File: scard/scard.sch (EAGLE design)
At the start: 7 parts, among them Q1 IRFD9210, X1 COAX

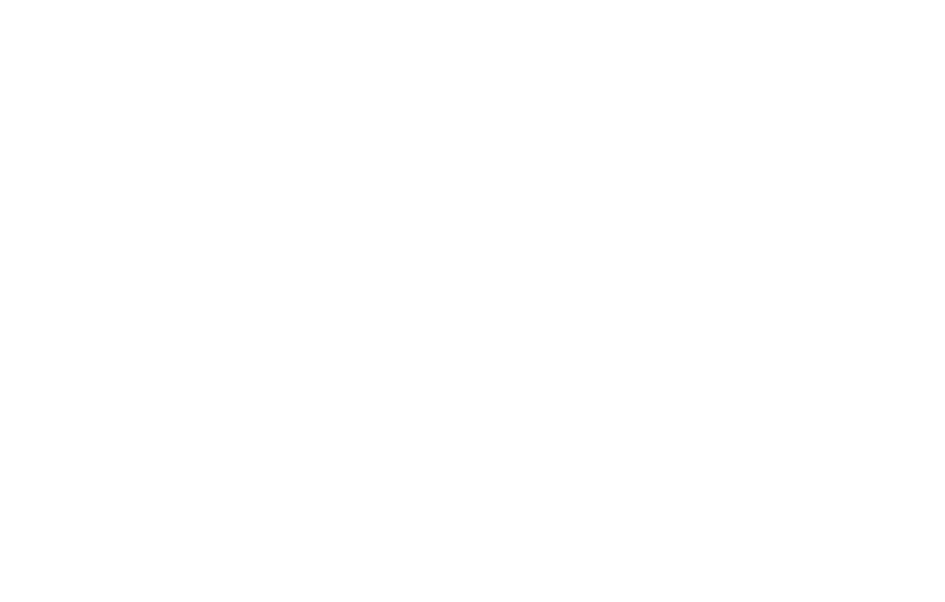
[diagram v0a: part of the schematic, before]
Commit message: added battery charging IC to library
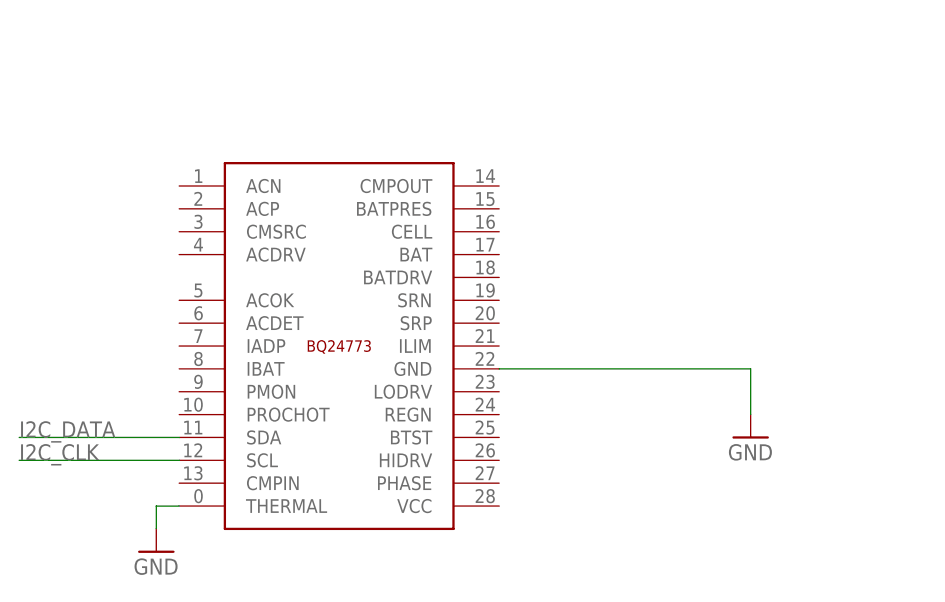
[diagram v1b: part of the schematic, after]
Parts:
- added BQ24773: BQ24773, calsat:BQ24773
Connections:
- new net I2C_CLK: BQ24773.SCL
- new net I2C_DATA: BQ24773.SDA
- net GND: now also BQ24773.GND@1, BQ24773.THERMAL
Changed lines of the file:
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@@
 <part name="GND4" library="supply1" library_urn="urn:adsk.eagle:library:371" deviceset="GND" device=""/>
 <part name="X1" library="con-samtec" library_urn="urn:adsk.eagle:library:184" deviceset="COAX" device=""/>
+<part name="BQ24773" library="calsat" deviceset="BQ24773" device=""/>
+<part name="GND5" library="supply1" library_urn="urn:adsk.eagle:library:371" deviceset="GND" device=""/>
+<part name="GND6" library="supply1" library_urn="urn:adsk.eagle:library:371" deviceset="GND" device=""/>
 </parts>
 <sheets>
@@
 <instance part="GND4" gate="1" x="-167.64" y="81.28"/>
 <instance part="X1" gate="COAX" x="-127" y="129.54"/>
+<instance part="BQ24773" gate="G$1" x="-134.62" y="-66.04"/>
+<instance part="GND5" gate="1" x="-88.9" y="-76.2"/>
+<instance part="GND6" gate="1" x="-154.94" y="-88.9"/>
 </instances>
 <busses>
@@
 <wire x1="-167.64" y1="83.82" x2="-167.64" y2="86.36" width="0.1524" layer="91"/>
 </segment>
+<segment>
+<pinref part="BQ24773" gate="G$1" pin="GND@1"/>
+<wire x1="-116.84" y1="-68.58" x2="-88.9" y2="-68.58" width="0.1524" layer="91"/>
+<wire x1="-88.9" y1="-68.58" x2="-88.9" y2="-73.66" width="0.1524" layer="91"/>
+<pinref part="GND5" gate="1" pin="GND"/>
+</segment>
+<segment>
+<pinref part="BQ24773" gate="G$1" pin="THERMAL"/>
+<pinref part="GND6" gate="1" pin="GND"/>
+<wire x1="-152.4" y1="-83.82" x2="-154.94" y2="-83.82" width="0.1524" layer="91"/>
+<wire x1="-154.94" y1="-83.82" x2="-154.94" y2="-86.36" width="0.1524" layer="91"/>
+</segment>
 </net>
 <net name="STS" class="0">
@@
 </segment>
 </net>
+<net name="I2C_DATA" class="0">
+<segment>
+<pinref part="BQ24773" gate="G$1" pin="SDA"/>
+<wire x1="-152.4" y1="-76.2" x2="-170.18" y2="-76.2" width="0.1524" layer="91"/>
+<label x="-170.18" y="-76.2" size="1.778" layer="95"/>
+</segment>
+</net>
+<net name="I2C_CLK" class="0">
+<segment>
+<pinref part="BQ24773" gate="G$1" pin="SCL"/>
+<wire x1="-152.4" y1="-78.74" x2="-170.18" y2="-78.74" width="0.1524" layer="91"/>
+<label x="-170.18" y="-78.74" size="1.778" layer="95"/>
+</segment>
+</net>

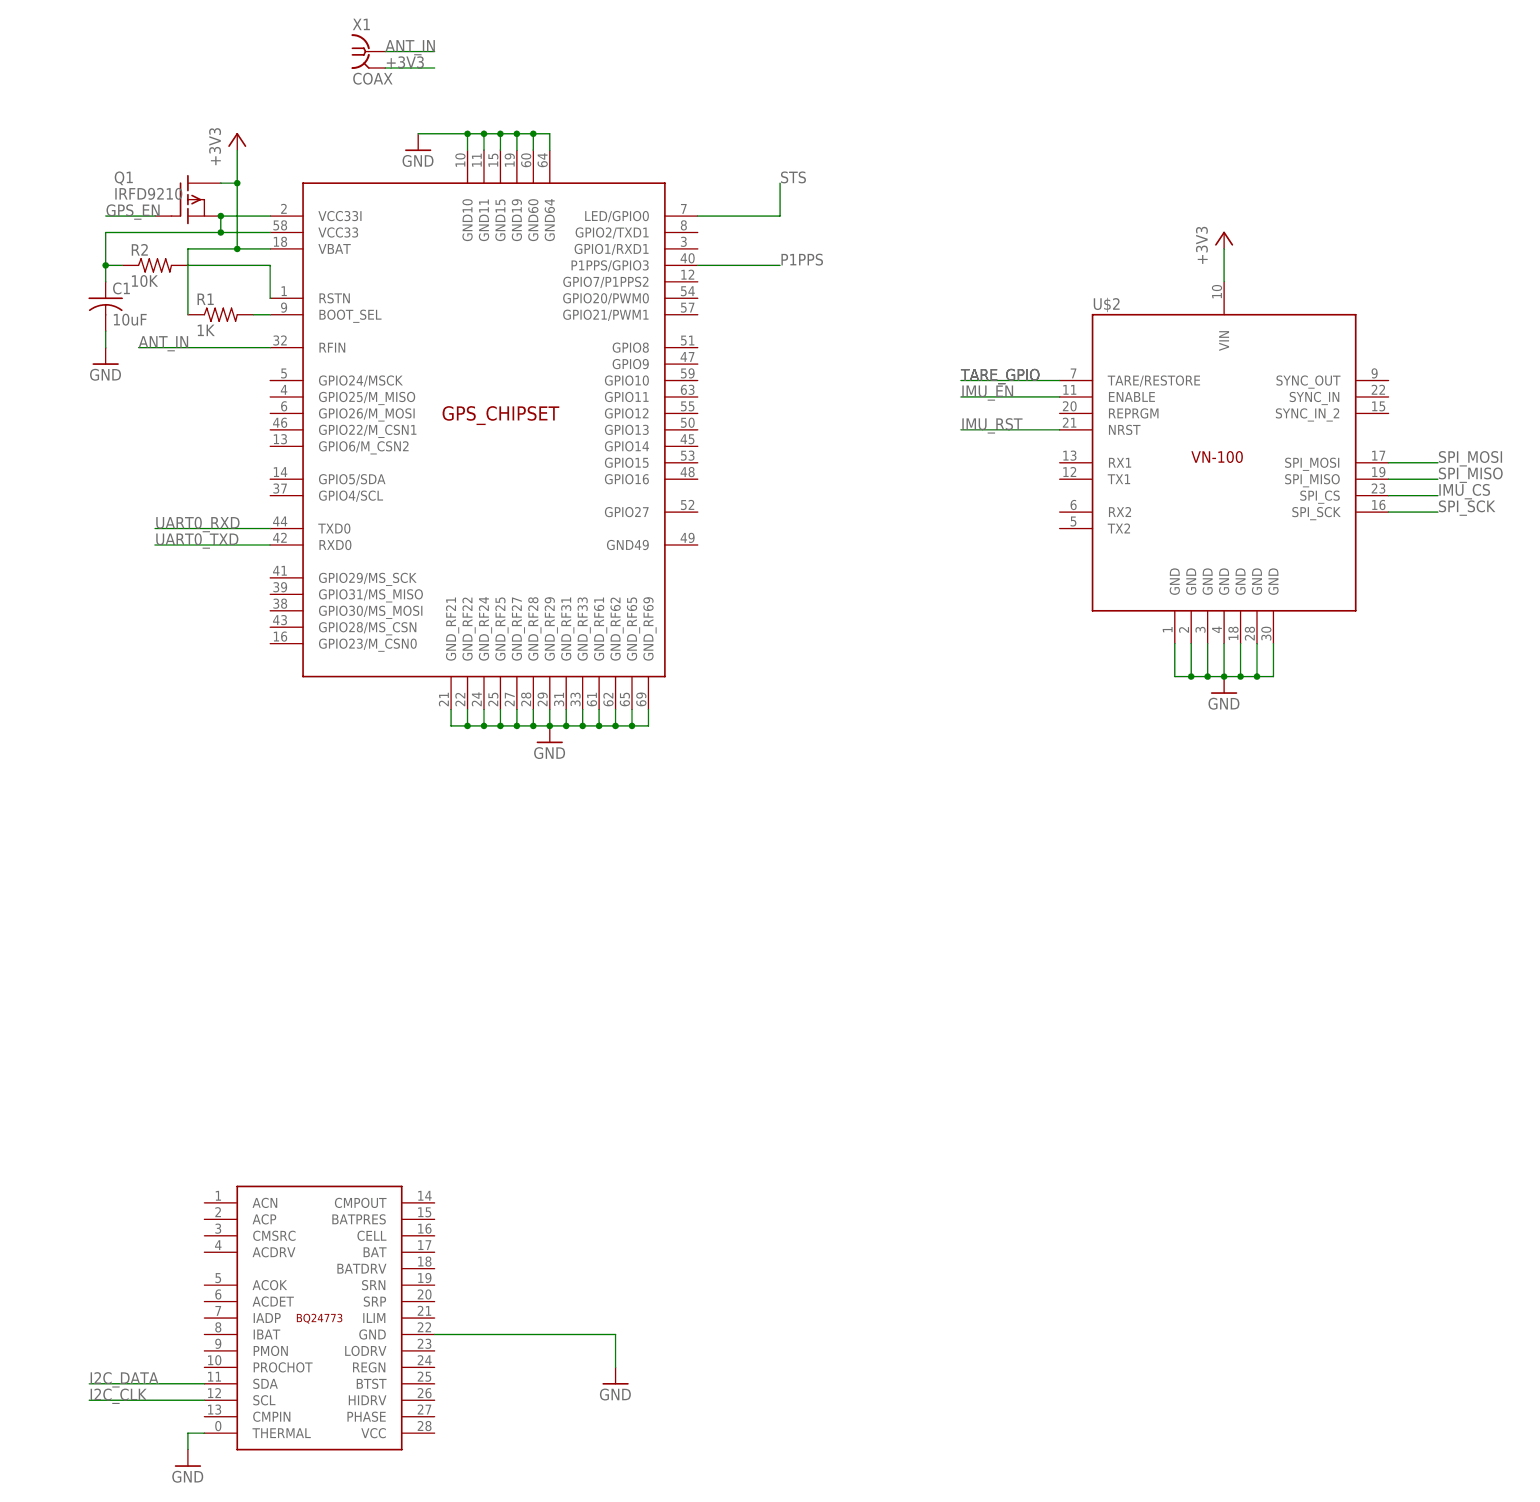
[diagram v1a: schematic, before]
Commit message: BQ24773 application circuit added
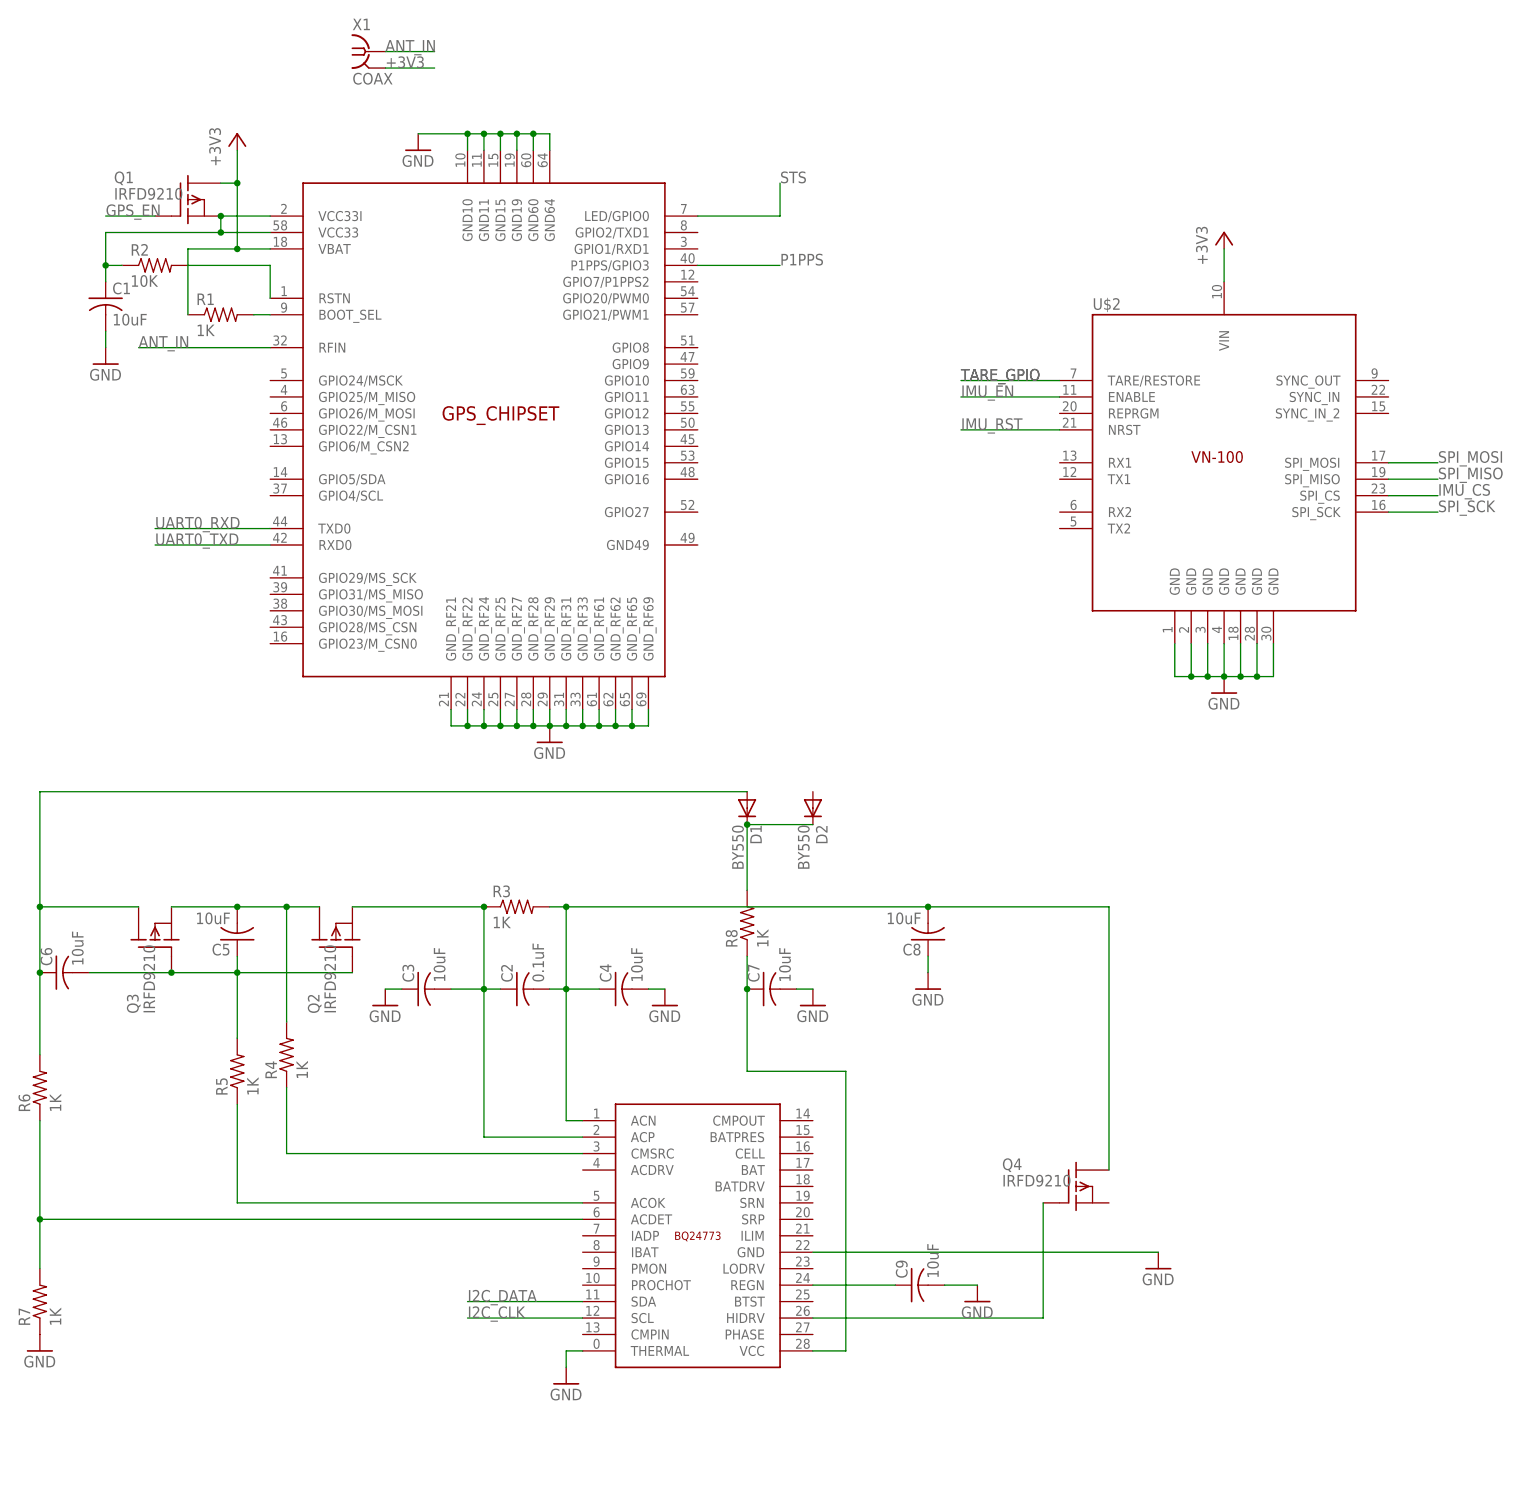
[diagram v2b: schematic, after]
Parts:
- added C2: 0.1uF, rcl:C-USC0603
- added C3, C4, C5, C6, C7, C8, C9: 10uF, rcl:C-USC0603
- added D1, D2: BY550, diode:BY550
- added Q2, Q3, Q4: IRFD9210, transistor-fet:IRFD9210
- added R3, R4, R5, R6, R7, R8: 1K, resistor:R-US_R0603
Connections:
- new net N$10: C6.1, D1.A, Q3.D, R6.2
- new net N$11: D1.C, D2.C, R8.2
- new net N$12: BQ24773.ACDET, R6.1, R7.2
- new net N$13: BQ24773.VCC, C7.1, R8.1
- new net N$14: BQ24773.REGN, C9.1
- new net N$15: BQ24773.HIDRV, Q4.G
- new net N$2: BQ24773.ACP, C2.1, C3.2, Q2.S, R3.1
- new net N$3: BQ24773.ACN, C2.2, C4.1, C8.2, Q4.D, R3.2
- new net N$4: BQ24773.CMSRC, R4.1
- new net N$5: BQ24773.ACOK, R5.1
- new net N$6: C5.1, C6.2, Q2.G, Q3.G, R5.2
- new net N$9: C5.2, Q2.D, Q3.S, R4.2
- net GND: now also C3.1, C4.2, C7.2, C8.1, C9.2
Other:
- moved on the sheet: BQ24773
